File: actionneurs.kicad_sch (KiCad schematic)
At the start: 50 parts, among them J1 EV_1, J12 LED_EN, J13 ESC_35_1_S, J14 ESC_35_2_S, J2 EV_2, J3 EV_3, J4 EV_P, J5 MOTOR_15_1, J6 MOTOR_15_2, J7 MOTOR_15_3, J8 ESC_35_1_P, J8 ESC_35_2_P, Q4 G2302, Q5 G2302, Q6 G2302, Q7 G2302, Q8 G2302, X1 ESC_Emax_Bullet_15A, X2 ESC_Emax_Bullet_15A, X3 ESC_Emax_Bullet_15A

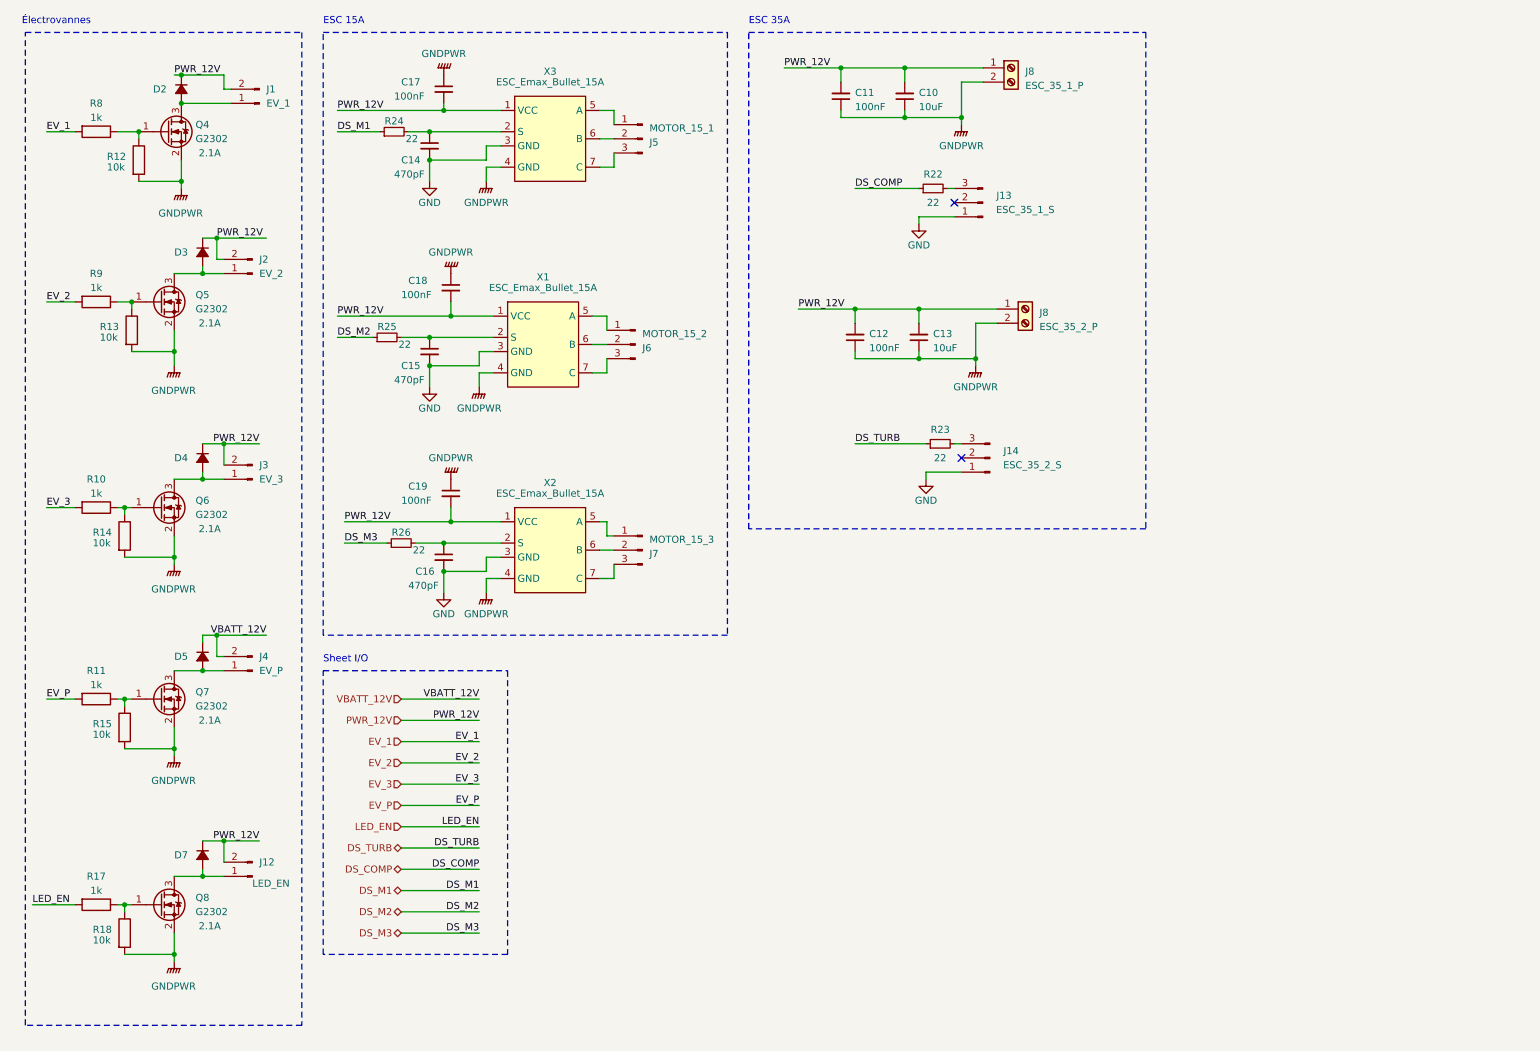
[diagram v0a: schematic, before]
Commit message: Few details -> add filtering on 35A ESC signals + 3.3V capa ...
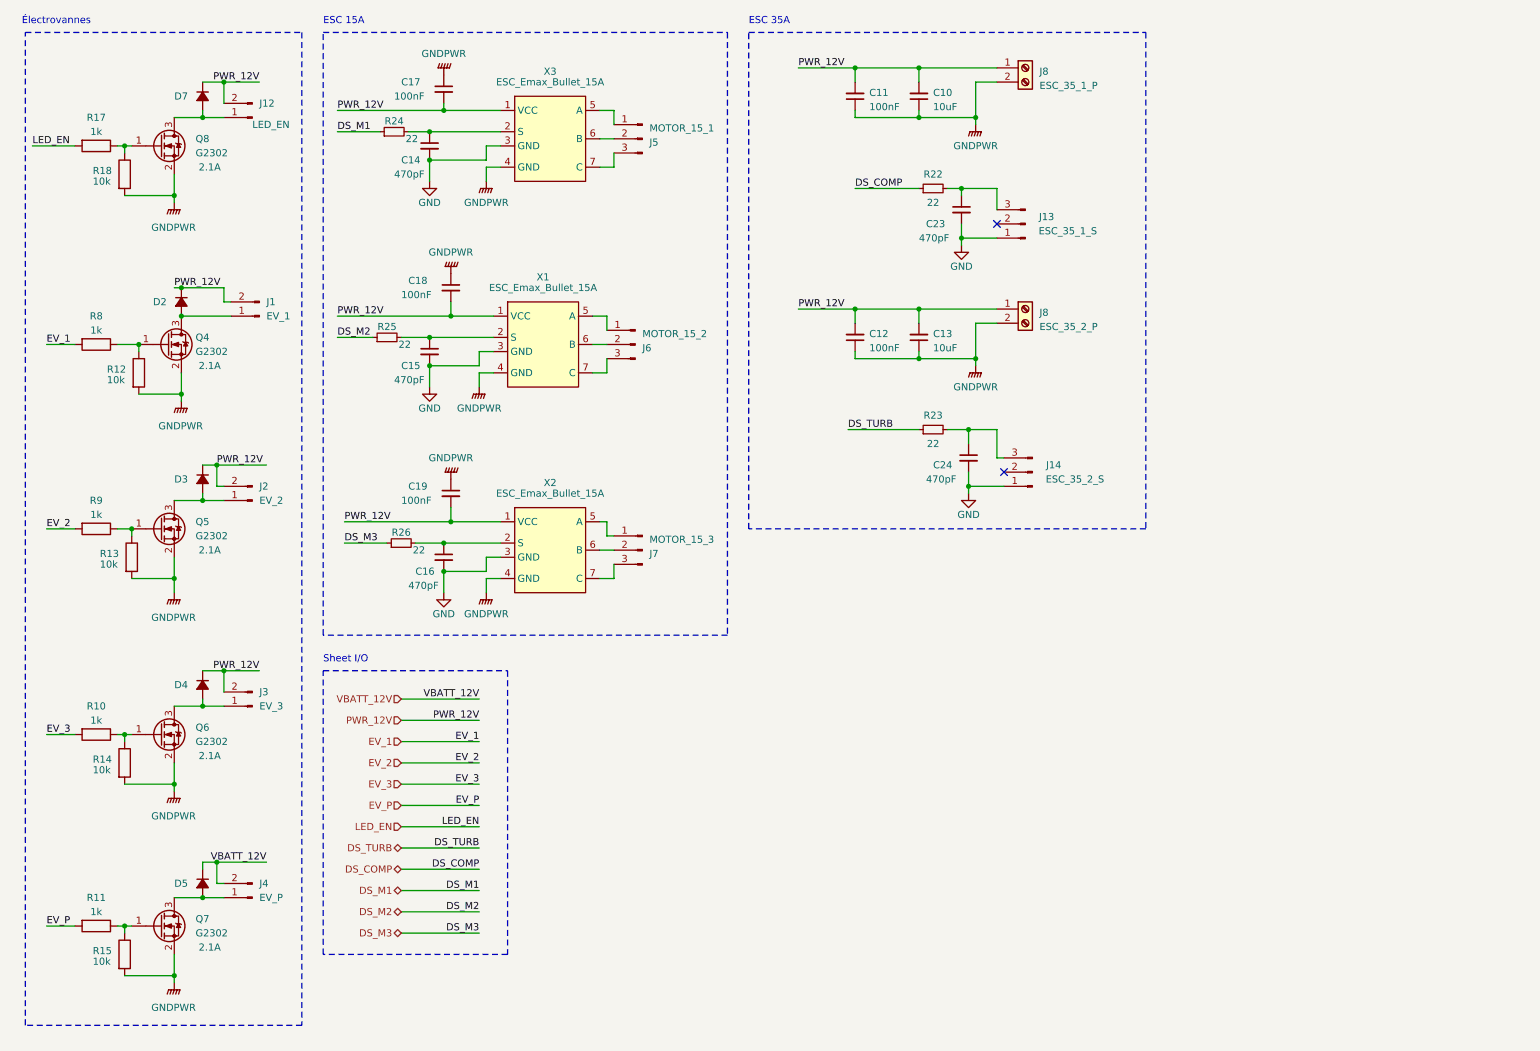
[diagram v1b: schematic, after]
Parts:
- added C23, C24: 470pF, Capacitor_SMD:C_0603_1608Metric, symbol Device:C_Small
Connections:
- net GND: now also C23.2, C24.2
- net at J13.3 (Pin_3), R22.2: now also C23.1
- net at J14.3 (Pin_3), R23.2: now also C24.1
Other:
- moved on the sheet: C10, C11, D2, D3, D4, D5, D7, J1, J12, J13, J14, J2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

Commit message: Schematics finished, reanotated sch
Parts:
- removed J1: EV_1, Connector_PinHeader_2.54mm:PinHeader_1x02_P2.54mm_Vertical, symbol Connector:Conn_01x02_Pin
- removed J2: EV_2, Connector_PinHeader_2.54mm:PinHeader_1x02_P2.54mm_Vertical, symbol Connector:Conn_01x02_Pin
- removed J3: EV_3, Connector_PinHeader_2.54mm:PinHeader_1x02_P2.54mm_Vertical, symbol Connector:Conn_01x02_Pin
- removed J4: EV_P, Connector_PinHeader_2.54mm:PinHeader_1x02_P2.54mm_Vertical, symbol Connector:Conn_01x02_Pin
- added J14: 690367280876, ConnectorsEvo:690367280876, symbol ConnectorsEvo:690367280876
- renumbered C18 to C10, C12 to C11, C13 to C12, C15 to C13, C24 to C14, C19 to C15, C17 to C5, C11 to C6, C10 to C7, C14 to C8, C23 to C9
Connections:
- net PWR_12V: now also J14.1, J14.3, J14.5, J14.7
- net 12V_EVP: now reaches D5.2 (A), Q7.3 (D)
- net 12V_EVP: now also J14.8
- net 12V_EV1: now reaches D2.2 (A), Q4.3 (D)
- net 12V_EV1: now also J14.2
- net 12V_EV2: now reaches D3.2 (A), Q5.3 (D)
- net 12V_EV2: now also J14.4
- net 12V_EV3: now reaches D4.2 (A), Q6.3 (D)
- net 12V_EV3: now also J14.6
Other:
- note added: "Connecteur EV"

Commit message: Update schematic pinout for LED_EN + Add mechanical constraints to PCB layout
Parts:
- C12, C7: footprint Capacitor_SMD:C_0805_2012Metric -> Capacitor_THT:CP_Radial_D5.0mm_P2.00mm
- D2, D3, D4, D5, D7: footprint Diode_SMD:D_SOD-323 -> Diode_SMD:D_SOD-123F
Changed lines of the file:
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@@
       (effects (font (size 1.27 1.27)) (justify left) hide)
     )
-    (property "Footprint" "Diode_SMD:D_SOD-323" (at 46.99 168.91 90)
+    (property "Footprint" "Diode_SMD:D_SOD-123F" (at 46.99 168.91 90)
       (effects (font (size 1.27 1.27)) hide)
     )
@@
       (effects (font (size 1.27 1.27)) (justify right))
     )
-    (property "Footprint" "Capacitor_SMD:C_0805_2012Metric" (at 175.26 71.12 0)
+    (property "Footprint" "Capacitor_THT:CP_Radial_D5.0mm_P2.00mm" (at 175.26 71.12 0)
       (effects (font (size 1.27 1.27)) hide)
     )
@@
       (effects (font (size 1.27 1.27)) (justify right))
     )
-    (property "Footprint" "Capacitor_SMD:C_0805_2012Metric" (at 175.26 27.94 0)
+    (property "Footprint" "Capacitor_THT:CP_Radial_D5.0mm_P2.00mm" (at 175.26 27.94 0)
       (effects (font (size 1.27 1.27)) hide)
     )
@@
       (effects (font (size 1.27 1.27)) (justify left) hide)
     )
-    (property "Footprint" "Diode_SMD:D_SOD-323" (at 46.99 133.35 90)
+    (property "Footprint" "Diode_SMD:D_SOD-123F" (at 46.99 133.35 90)
       (effects (font (size 1.27 1.27)) hide)
     )
@@
       (effects (font (size 1.27 1.27)) (justify left) hide)
     )
-    (property "Footprint" "Diode_SMD:D_SOD-323" (at 43.18 64.77 90)
+    (property "Footprint" "Diode_SMD:D_SOD-123F" (at 43.18 64.77 90)
       (effects (font (size 1.27 1.27)) hide)
     )
@@
       (effects (font (size 1.27 1.27)) (justify left) hide)
     )
-    (property "Footprint" "Diode_SMD:D_SOD-323" (at 46.99 27.94 90)
+    (property "Footprint" "Diode_SMD:D_SOD-123F" (at 46.99 27.94 90)
       (effects (font (size 1.27 1.27)) hide)
     )
@@
       (effects (font (size 1.27 1.27)) (justify left) hide)
     )
-    (property "Footprint" "Diode_SMD:D_SOD-323" (at 46.99 96.52 90)
-      (effects (font (size 1.27 1.27)) hide)
-    )
+    (property "Footprint" "Diode_SMD:D_SOD-123F" (at 46.99 96.52 90)
+      (effects (font (size 1.27 1.27)) hide)
+    )

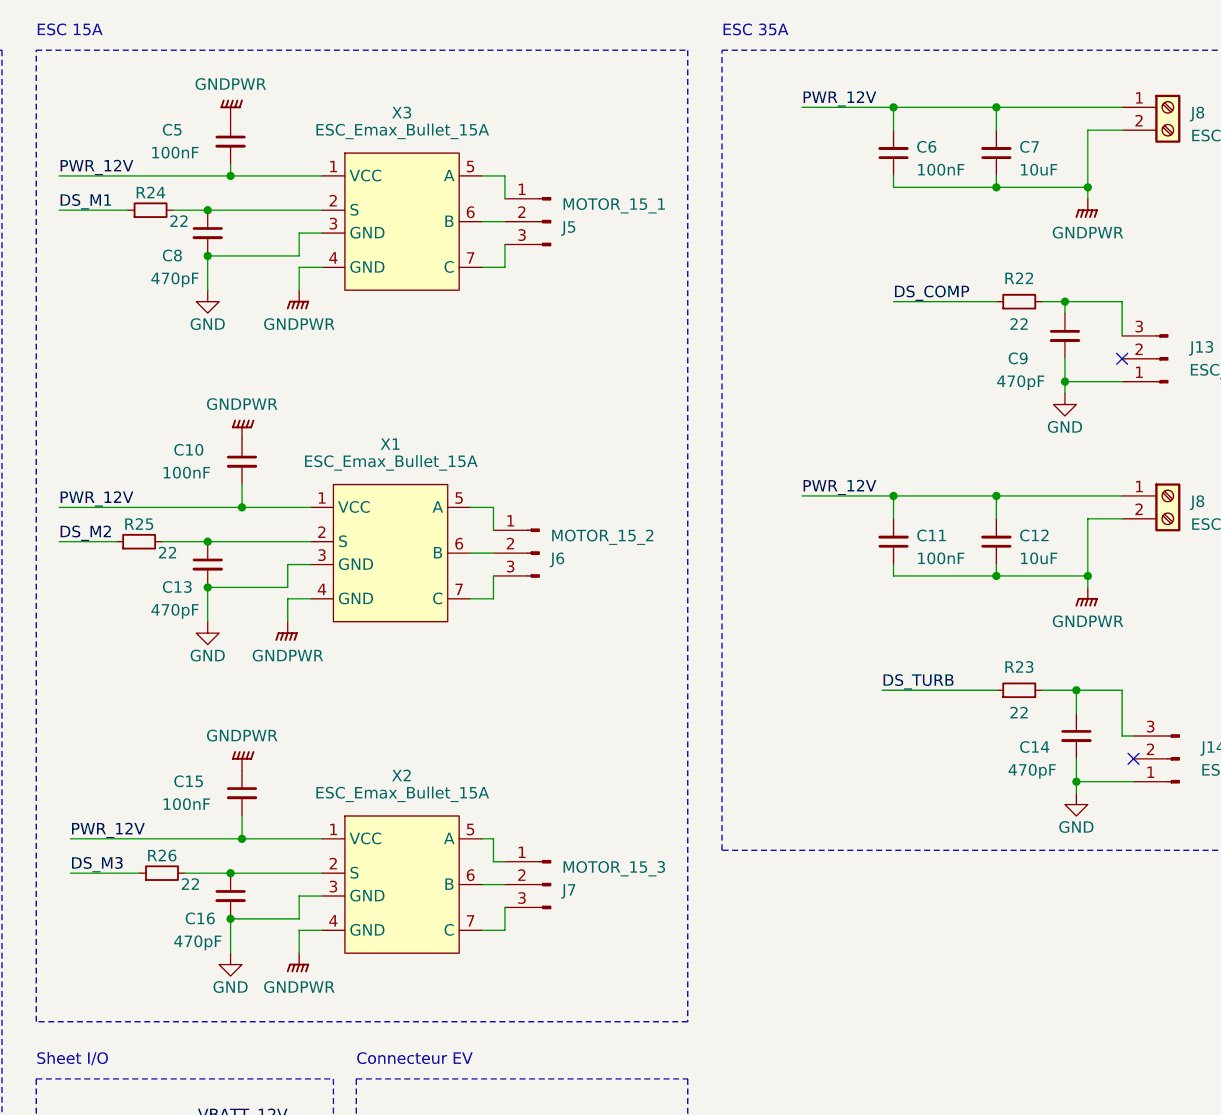
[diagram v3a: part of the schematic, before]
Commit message: Before making power planes
Signal routing done. Added I2C level shifter in schematics.
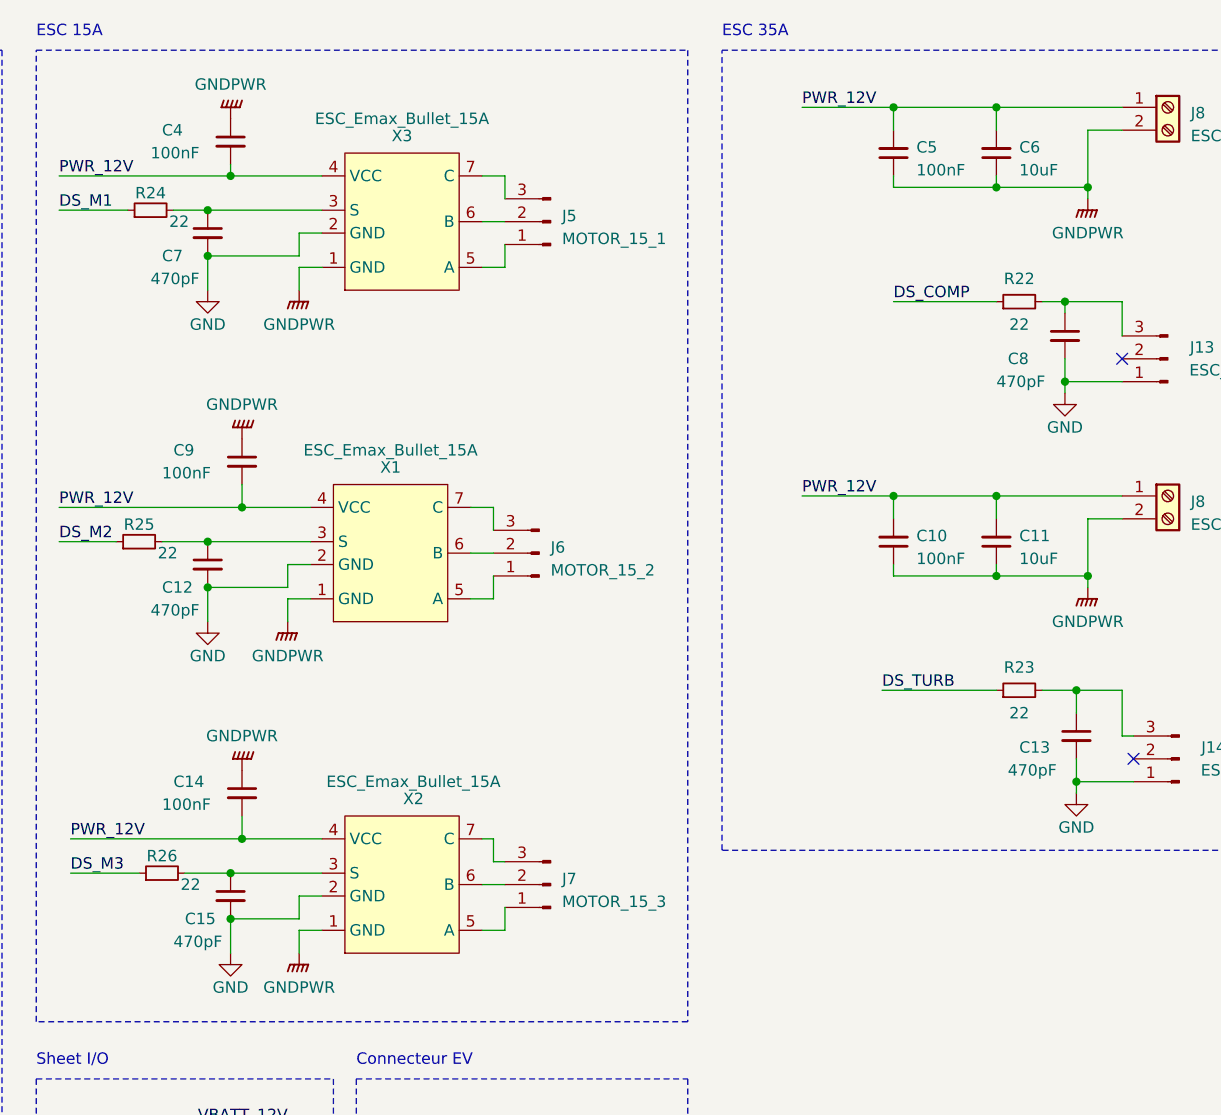
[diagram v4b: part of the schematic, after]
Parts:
- renumbered C11 to C10, C12 to C11, C13 to C12, C14 to C13, C15 to C14, C16 to C15, C5 to C4, C6 to C5, C7 to C6, C8 to C7, C9 to C8, C10 to C9
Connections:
- net GND: now also X1.2 (GND), X2.2 (GND), X3.2 (GND); no longer X1.3 (GND), X2.3 (GND), X3.3 (GND)
- net GNDPWR: now also X1.1 (GND), X2.1 (GND), X3.1 (GND); no longer X1.4 (GND), X2.4 (GND), X3.4 (GND)
- net PWR_12V: now also X1.4 (VCC), X2.4 (VCC), X3.4 (VCC); no longer X1.1 (VCC), X2.1 (VCC), X3.1 (VCC)
- net at C7.1, R24.2: now also X3.3 (S); no longer X3.2 (S)
- net at C15.1, R26.2: now also X2.3 (S); no longer X2.2 (S)
- net at C12.1, R25.2: now also X1.3 (S); no longer X1.2 (S)
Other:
- moved on the sheet: J5, J6, J7

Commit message: PCB finished
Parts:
- C11, C6: symbol Device:C_Small -> Device:C_Polarized_Small
- J8: value ESC_35_2_P -> ESC_35_1_P
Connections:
- net GNDPWR: now also C11.2, C6.2; no longer C11.1, C6.1
- net PWR_12V: now also C11.1, C6.1; no longer C11.2, C6.2
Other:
- moved on the sheet: C10, C5, J8

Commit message: CDR 2025 version WIP
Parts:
- removed C12, C15, C7: 470pF, Capacitor_SMD:C_0603_1608Metric, symbol Device:C_Small
- removed C14, C4, C9: 100nF, Capacitor_SMD:C_0603_1608Metric, symbol Device:C_Small
- removed D7: ~, Diode_SMD:D_SOD-123F, symbol Device:D_Small_Filled
- removed J12: LED_EN, Connector_PinHeader_2.54mm:PinHeader_1x02_P2.54mm_Vertical, symbol Connector:Conn_01x02_Pin
- removed J5: MOTOR_15_1, Connector_PinHeader_2.54mm:PinHeader_1x03_P2.54mm_Vertical, symbol Connector:Conn_01x03_Pin
- removed J6: MOTOR_15_2, Connector_PinHeader_2.54mm:PinHeader_1x03_P2.54mm_Vertical, symbol Connector:Conn_01x03_Pin
- removed Q8: G2302, Package_TO_SOT_SMD:SOT-23, symbol Device:Q_NMOS_GSD
- removed R17: 1k, Resistor_SMD:R_0603_1608Metric, symbol Device:R
- removed R18: 10k, Resistor_SMD:R_0603_1608Metric, symbol Device:R
- removed R24, R25, R26: 22, Resistor_SMD:R_0603_1608Metric, symbol Device:R_Small
- removed X1, X2, X3: ESC_Emax_Bullet_15A, ComponentsEvo:ESC_Emax_Bullet_15A, symbol ComponentsEvo:ESC_Emax_Bullet_15A
- added D10, D11, D12, D13, D14, D15, D16, D17, D18: ~, Diode_SMD:D_SOD-123F, symbol Device:D_Small_Filled
- added J1, J11: 690367280876, ConnectorsEvo:690367280876, symbol ConnectorsEvo:690367280876
- added Q1, Q10, Q11, Q12, Q13, Q14, Q15, Q16, Q17, Q9: G2302, Package_TO_SOT_SMD:SOT-23, symbol Device:Q_NMOS_GSD
- added R12, R34, R36, R37, R38, R39, R40, R41, R51: 1k, Resistor_SMD:R_0603_1608Metric, symbol Device:R
- added R33, R35, R42, R43, R44, R45, R46, R47, R52: 10k, Resistor_SMD:R_0603_1608Metric, symbol Device:R
- added R48: 10k, Resistor_SMD:R_0603_1608Metric, symbol Device:R_Small
- added R49: 0, Resistor_SMD:R_0603_1608Metric, symbol Device:R_Small
- added R50: 22, Resistor_SMD:R_0603_1608Metric, symbol Device:R_Small
- J7: value MOTOR_15_3 -> RGBA_LEDs
- R10: renamed from R23; now not fitted; now left out of the parts list
- renumbered J8 to J10, J14 to J12, J8 to J6, J13 to J9, Q4 to Q2, Q5 to Q3, Q6 to Q4, Q7 to Q5, R9 to R11, R10 to R14, R14 to R15, R11 to R16, R15 to R17, R22 to R6, R12 to R9
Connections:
- net DS_TURB: now also R50.1
- net GNDPWR: now also J7.3 (Pin_3), Q1.2 (S), Q10.2 (S), Q11.2 (S), Q12.2 (S), Q13.2 (S), Q14.2 (S), Q15.2 (S), Q16.2 (S), Q17.2 (S), Q9.2 (S), R33.2, R35.2, R42.2, R43.2, R44.2, R45.2, R46.2, R47.2, R48.1, R49.1, R52.2; no longer J6.2 (Pin_2)
- net PWR_12V: now also D10.1 (K), D11.1 (K), D12.1 (K), D13.1 (K), D14.1 (K), D15.1 (K), D16.1 (K), D17.1 (K), D18.1 (K), J1.1, J1.3, J1.5, J1.7, J11.1, J11.3, J11.5, J11.7; no longer J14.7
- net +5VP: now reaches J7.1 (Pin_1)
- net DATA_LED: now reaches J7.2 (Pin_2)
- net VBATT_12V renamed VBAT_12V
- net VBAT_12V: now also J14.7
- new net: Q11.1 (G), R38.1, R42.1
- new net: Q10.1 (G), R37.1, R46.1
- new net: Q1.1 (G), R12.1, R33.1
- new net: Q9.1 (G), R34.1, R35.1
- new net: Q13.1 (G), R40.1, R44.1
- new net: Q14.1 (G), R41.1, R45.1
- new net: Q16.1 (G), R48.2, R50.2
- new net: J6.2 (Pin_2), Q16.3 (D), R49.2
- new net: Q17.1 (G), R51.1, R52.1
- new net: Q12.1 (G), R39.1, R43.1
- new net: Q15.1 (G), R36.1, R47.1
- new net 12V_EV10: D16.2 (A), J11.6, Q13.3 (D)
- new net 12V_EV11: D17.2 (A), J11.8, Q14.3 (D)
- new net 12V_EV4: D10.2 (A), J1.2, Q1.3 (D)
- new net 12V_EV5: D11.2 (A), J1.4, Q9.3 (D)
- new net 12V_EV6: D12.2 (A), J1.6, Q15.3 (D)
- new net 12V_EV7: D13.2 (A), J1.8, Q10.3 (D)
- new net 12V_EV8: D14.2 (A), J11.2, Q11.3 (D)
- new net 12V_EV9: D15.2 (A), J11.4, Q12.3 (D)
- new net 12V_VAC: D18.2 (A), Q17.3 (D)
- new net EV_10: R40.2
- new net EV_11: R41.2
- new net EV_4: R12.2
- new net EV_5: R34.2
- new net EV_6: R36.2
- new net EV_7: R37.2
- new net EV_8: R38.2
- new net EV_9: R39.2
- new net VAC: R51.2
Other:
- note added: "3A max"
- note added: "BLDC -> 30A max."
- note added: "Contrôle LEDs adressables"
- note added: "ESC Compresseur"
- note added: "Pompe à vide"
- note added: "R50 + Q16 = Commutation 12V OU R10 + R49 = 12V + PWM (ESC)"
- note removed: "ESC 15A"
- note removed: "ESC 35A"
- moved on the sheet: C10, C11, C13, C5, C6, C8, D2, D3, D4, D5, J10, J12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
